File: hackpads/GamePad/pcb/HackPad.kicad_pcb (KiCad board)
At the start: 2 copper layers, 100 x 69 mm, 36 parts, among them J1 OLED_128x64, SW1 SW_Push_45deg, SW10 RotaryEncoder_Switch, SW2 SW_Push_45deg, SW3 SW_Push_45deg, SW4 SW_Push_45deg, SW5 SW_Push_45deg, SW6 SW_Push_45deg, SW7 SW_Push_45deg, SW8 SW_Push_45deg, U1 MOUDLE-SEEEDUINO-XIAO

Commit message: minor edits
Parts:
- moved G*** 0.50 mm to (180.0, 90.5)
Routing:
- net Row 3: track 152.4 -> 160.1 mm, vias 1 -> 0
- net Net-(D16-DOUT): track 74.0 -> 71.7 mm
- net Column 2: track 126.1 -> 127.0 mm
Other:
- board text added: ")"
- board text added: ":"
- board text added: "Thanks Alex!"
- board text removed: "Thanks Alex! :)"

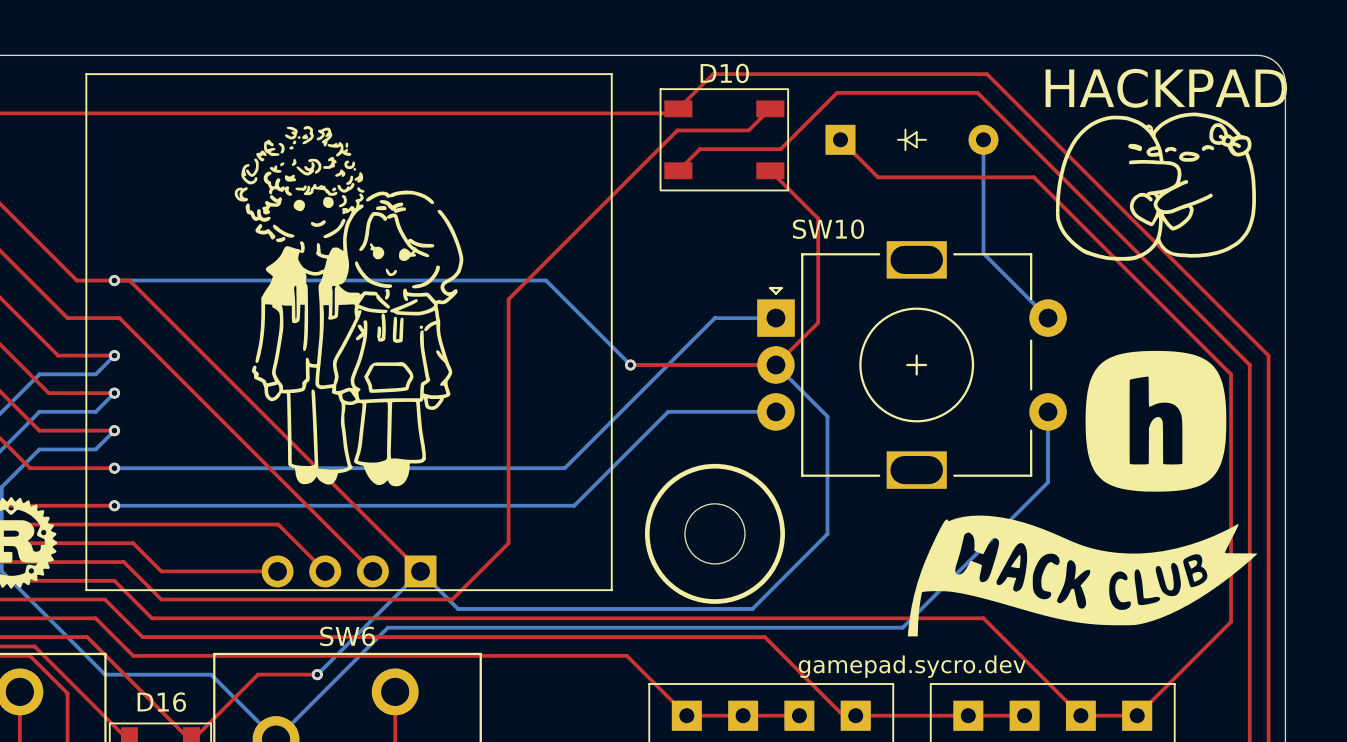
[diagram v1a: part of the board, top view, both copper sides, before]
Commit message: move the rotary encoder right
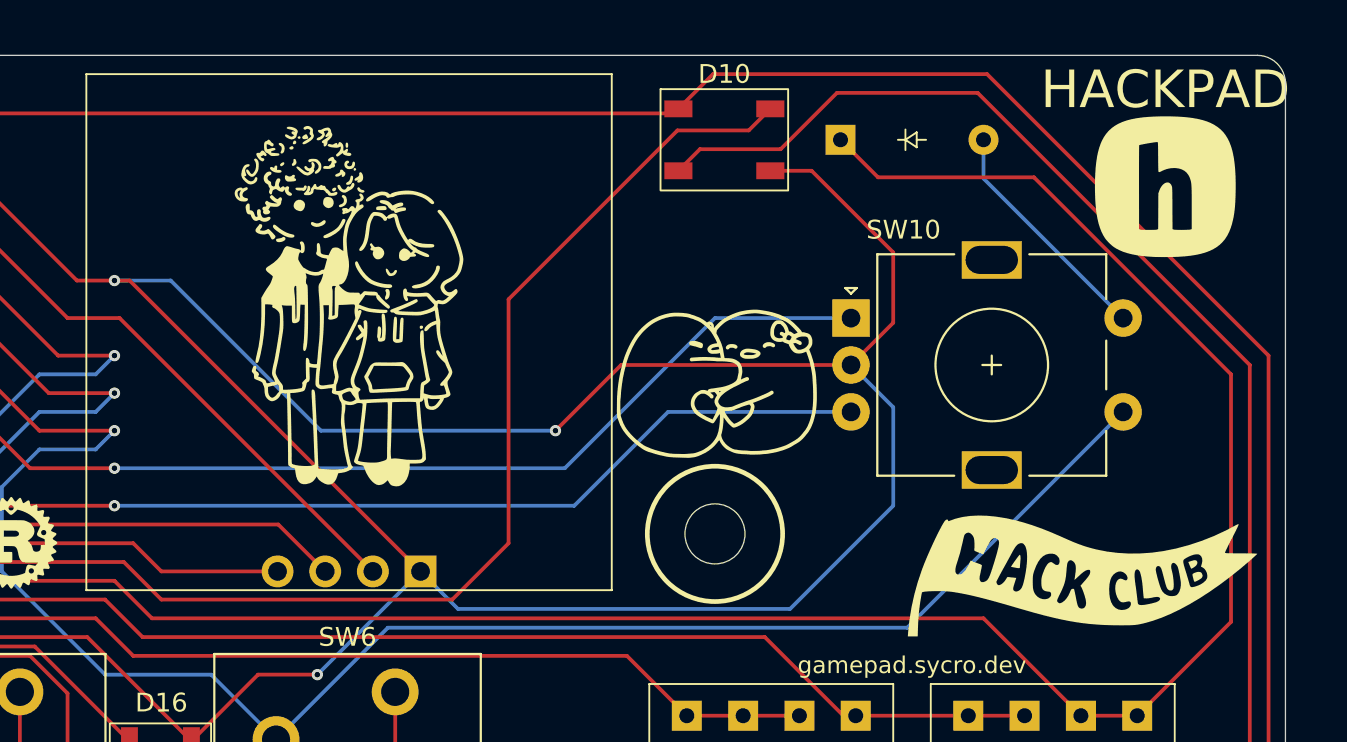
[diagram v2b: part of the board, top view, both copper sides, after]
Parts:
- moved G*** 25.6 mm to (156.8, 87.5)
- moved G*** 12.5 mm to (180.5, 78.0)
- moved SW10 4.00 mm to (163.8, 85.0)
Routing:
- net GND: track 278.2 -> 289.8 mm
- net EC11B: track 75.4 -> 79.4 mm
- net EC11A: track 51.9 -> 55.9 mm
- net Column 3: track 115.0 -> 116.8 mm
- net EC11SWB: track 10.9 -> 12.6 mm
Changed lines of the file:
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@@
 	(footprint "LOGO"
 		(layer "F.Cu")
-		(at 180 90.5)
+		(at 180.5 78)
 		(property "Reference" "G***"
 			(at 0 0 0)
@@
 	(footprint "LOGO"
 		(layer "F.Cu")
-		(at 180.215771 77.038707)
+		(at 156.815771 87.538707)
 		(property "Reference" "G***"
 			(at 0 0 0)
@@
 	(footprint "Rotary_Encoder:RotaryEncoder_Alps_EC11E-Switch_Vertical_H20mm"
 		(layer "F.Cu")
-		(at 159.75 85)
+		(at 163.75 85)
 		(descr "Alps rotary encoder, EC12E... with switch, vertical shaft, http://www.alps.com/prod/info/E/HTML/Encoder/Incremental/EC11/EC11E15204A3.html")
 		(tags "rotary encoder")
@@
 	)
 	(segment
-		(start 174.25 85)
-		(end 170.81 81.56)
+		(start 178.25 85)
+		(end 170.81 77.56)
 		(width 0.2)
 		(layer "B.Cu")
@@
 	)
 	(segment
-		(start 170.81 81.56)
+		(start 170.81 77.56)
 		(end 170.81 75.5)
 		(width 0.2)
@@
 	)
 	(segment
-		(start 162 85.25)
-		(end 159.75 87.5)
-		(width 0.2)
-		(layer "F.Cu")
-		(net 15)
-	)
-	(segment
 		(start 114.625 76.632015)
 		(end 110.492985 72.5)
@@
 	)
 	(segment
+		(start 163.75 87.5)
+		(end 151.5 87.5)
+		(width 0.2)
+		(layer "F.Cu")
+		(net 15)
+	)
+	(segment
 		(start 136.753402 126.51)
 		(end 136.193402 125.95)
@@
 	)
 	(segment
-		(start 162 79.7)
-		(end 162 85.25)
-		(width 0.2)
-		(layer "F.Cu")
-		(net 15)
-	)
-	(segment
 		(start 123.05 102)
 		(end 128.6 107.55)
@@
 	)
 	(segment
+		(start 166 81.5)
+		(end 166 85.25)
+		(width 0.2)
+		(layer "F.Cu")
+		(net 15)
+	)
+	(segment
 		(start 150.7 125.5)
 		(end 148.65 127.55)
@@
 	)
 	(segment
+		(start 166 85.25)
+		(end 163.75 87.5)
+		(width 0.2)
+		(layer "F.Cu")
+		(net 15)
+	)
+	(segment
 		(start 162.5 127)
 		(end 157.592412 127)
@@
 	)
 	(segment
-		(start 110.29 125.91)
-		(end 108.65 127.55)
+		(start 151.5 87.5)
+		(end 148 91)
 		(width 0.2)
 		(layer "F.Cu")
@@
 	)
 	(segment
-		(start 120.053048 126.558984)
-		(end 114.441016 126.558984)
+		(start 110.29 125.91)
+		(end 108.65 127.55)
 		(width 0.2)
 		(layer "F.Cu")
@@
 	)
 	(segment
-		(start 159.75 87.5)
-		(end 152 87.5)
+		(start 120.053048 126.558984)
+		(end 114.441016 126.558984)
 		(width 0.2)
 		(layer "F.Cu")
@@
 	)
 	(segment
+		(start 161.65 77.15)
+		(end 166 81.5)
+		(width 0.2)
+		(layer "F.Cu")
+		(net 15)
+	)
+	(segment
 		(start 148.65 127.55)
 		(end 147.6 126.5)
@@
 	)
 	(segment
-		(start 159.45 77.15)
-		(end 162 79.7)
+		(start 108 117)
+		(end 108 108.3)
 		(width 0.2)
 		(layer "F.Cu")
@@
 	)
 	(segment
-		(start 108 117)
-		(end 108 108.3)
+		(start 125.31 83)
+		(end 140.81 98.5)
 		(width 0.2)
 		(layer "F.Cu")
@@
 	)
 	(segment
-		(start 125.31 83)
-		(end 140.81 98.5)
+		(start 159.45 77.15)
+		(end 161.65 77.15)
 		(width 0.2)
 		(layer "F.Cu")
@@
 	)
 	(via
-		(at 152 87.5)
+		(at 148 91)
 		(size 0.6)
 		(drill 0.3)
@@
 	)
 	(segment
-		(start 147.5 83)
-		(end 124.5 83)
+		(start 148 91)
+		(end 135.5 91)
 		(width 0.2)
 		(layer "B.Cu")
@@
 	)
 	(segment
-		(start 158.5 100.5)
-		(end 142.81 100.5)
+		(start 142.81 100.5)
+		(end 160.5 100.5)
 		(width 0.2)
 		(layer "B.Cu")
@@
 	)
 	(segment
-		(start 162.5 90.25)
-		(end 162.5 96.5)
+		(start 166 95)
+		(end 166 89.75)
 		(width 0.2)
 		(layer "B.Cu")
@@
 	)
 	(segment
-		(start 142.81 100.5)
-		(end 140.81 98.5)
+		(start 135.5 91)
+		(end 127.5 83)
 		(width 0.2)
 		(layer "B.Cu")
@@
 	)
 	(segment
-		(start 159.75 87.5)
-		(end 159 87.5)
+		(start 140.81 98.5)
+		(end 142.81 100.5)
 		(width 0.2)
 		(layer "B.Cu")
@@
 	)
 	(segment
-		(start 152 87.5)
-		(end 147.5 83)
+		(start 127.5 83)
+		(end 124.5 83)
 		(width 0.2)
 		(layer "B.Cu")
@@
 	)
 	(segment
-		(start 162.5 96.5)
-		(end 158.5 100.5)
+		(start 160.5 100.5)
+		(end 166 95)
 		(width 0.2)
 		(layer "B.Cu")
@@
 	)
 	(segment
-		(start 159.75 87.5)
-		(end 162.5 90.25)
+		(start 108 123)
+		(end 108 117)
 		(width 0.2)
 		(layer "B.Cu")
@@
 	)
 	(segment
-		(start 108 123)
-		(end 108 117)
+		(start 166 89.75)
+		(end 163.75 87.5)
 		(width 0.2)
 		(layer "B.Cu")
@@
 	)
 	(segment
-		(start 129.65 104)
+		(start 139.07 101.5)
 		(end 133.11 107.46)
 		(width 0.2)
@@
 	)
 	(segment
-		(start 124.5 91)
-		(end 123.5 92)
+		(start 129.65 104)
+		(end 133.11 107.46)
 		(width 0.2)
 		(layer "B.Cu")
@@
 	)
 	(segment
-		(start 174.25 93.75)
-		(end 166.5 101.5)
+		(start 124.5 91)
+		(end 123.5 92)
 		(width 0.2)
 		(layer "B.Cu")
@@
 	)
 	(segment
-		(start 139.07 101.5)
-		(end 133.11 107.46)
+		(start 178.25 90)
+		(end 166.75 101.5)
 		(width 0.2)
 		(layer "B.Cu")
@@
 	)
 	(segment
-		(start 123.5 92)
-		(end 120.5 92)
+		(start 166.75 101.5)
+		(end 139.07 101.5)
 		(width 0.2)
 		(layer "B.Cu")
@@
 	)
 	(segment
-		(start 174.25 90)
-		(end 174.25 93.75)
+		(start 123.5 92)
+		(end 120.5 92)
 		(width 0.2)
 		(layer "B.Cu")
@@
 	)
 	(segment
-		(start 166.5 101.5)
-		(end 139.07 101.5)
-		(width 0.2)
-		(layer "B.Cu")
-		(net 23)
-	)
-	(segment
 		(start 96 95)
 		(end 124.5 95)
@@
 	)
 	(segment
-		(start 149 95)
-		(end 154 90)
+		(start 154 90)
+		(end 163.75 90)
 		(width 0.2)
 		(layer "B.Cu")
@@
 	)
 	(segment
-		(start 124.5 95)
-		(end 149 95)
+		(start 149 95)
+		(end 154 90)
 		(width 0.2)
 		(layer "B.Cu")
@@
 	)
 	(segment
-		(start 154 90)
-		(end 159.75 90)
+		(start 124.5 95)
+		(end 149 95)
 		(width 0.2)
 		(layer "B.Cu")
@@
 	)
 	(segment
-		(start 156.5 85)
-		(end 159.75 85)
+		(start 124.5 93)
+		(end 148.5 93)
 		(width 0.2)
 		(layer "B.Cu")
@@
 	)
 	(segment
-		(start 124.5 93)
-		(end 148.5 93)
+		(start 156.5 85)
+		(end 163.75 85)
 		(width 0.2)
 		(layer "B.Cu")

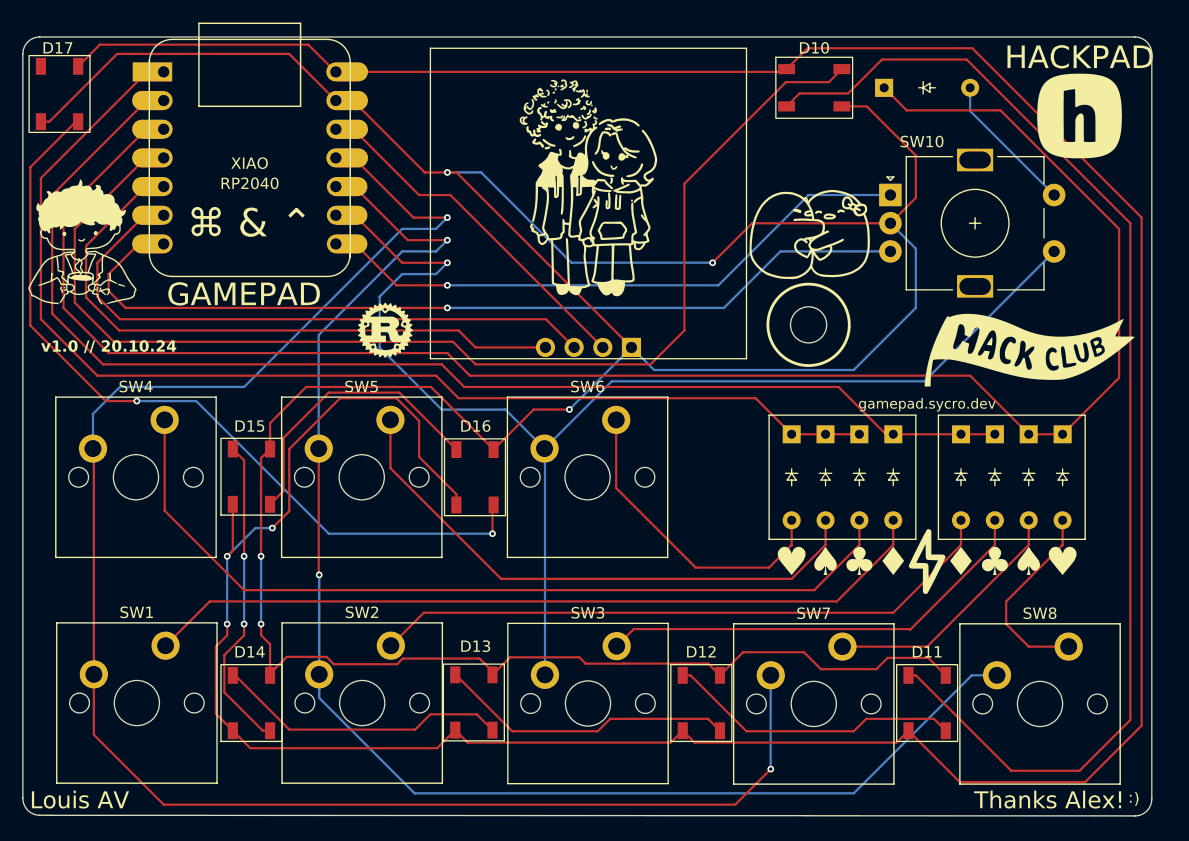
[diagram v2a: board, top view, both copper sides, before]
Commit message: fix the pin height issue
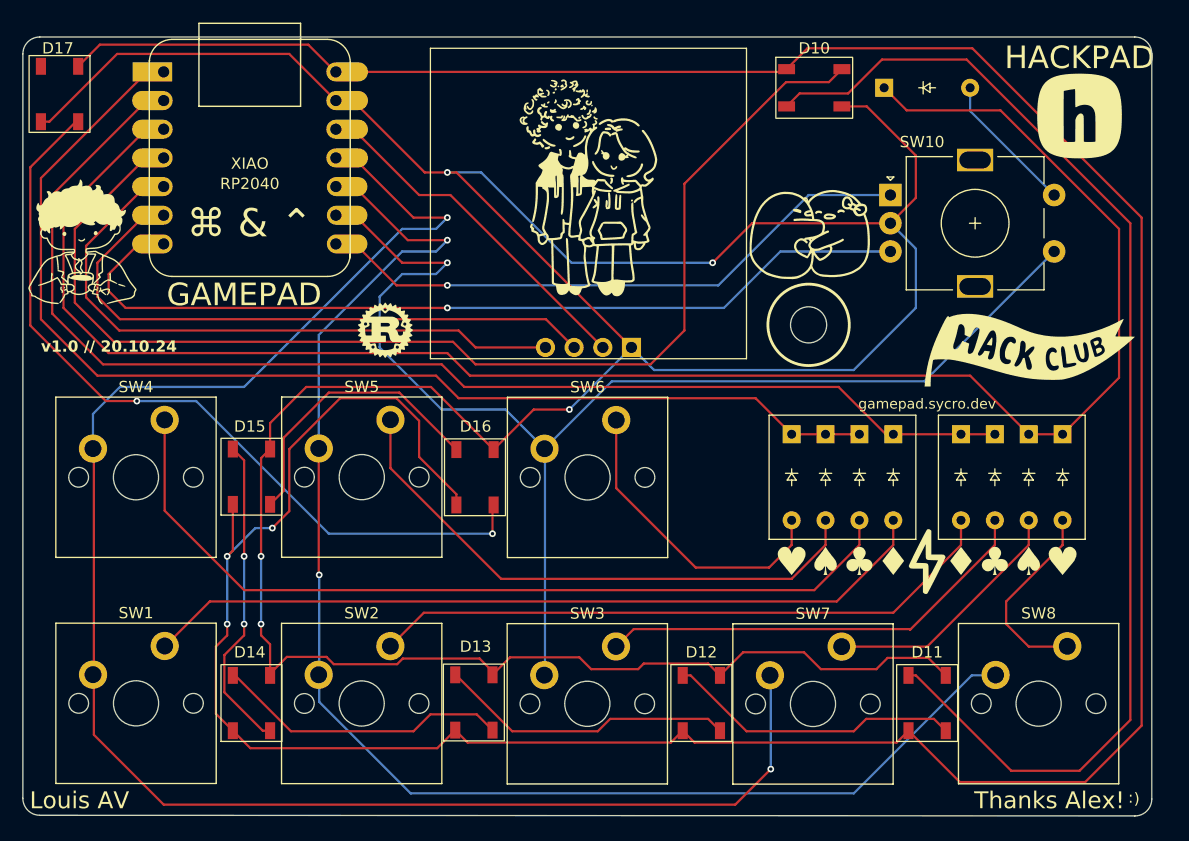
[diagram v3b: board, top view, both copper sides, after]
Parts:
- moved SW8 0.13 mm to (176.9, 130.1)
- moved SW1 0.08 mm to (96.9, 130.0)
- moved SW7 0.07 mm to (156.9, 130.1)
- moved SW3 0.07 mm to (136.9, 130.1)
- moved SW2 0.06 mm to (116.9, 130.0)
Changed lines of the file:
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@@
 		(pad_to_mask_clearance 0)
 		(allow_soldermask_bridges_in_footprints no)
+		(grid_origin 86.9 71)
 		(pcbplotparams
 			(layerselection 0x00010fc_ffffffff)
@@
 	(footprint "ScottoKeebs_MX:MX_PCB_1.00u"
 		(layer "F.Cu")
-		(at 156.96 130.08)
+		(at 156.8875 130.08)
 		(descr "MX keyswitch PCB Mount Keycap 1.00u")
 		(tags "MX Keyboard Keyswitch Switch PCB Cutout Keycap 1.00u")
@@
 	(footprint "ScottoKeebs_MX:MX_PCB_1.00u"
 		(layer "F.Cu")
-		(at 97 130)
+		(at 96.925 130.025)
 		(descr "MX keyswitch PCB Mount Keycap 1.00u")
 		(tags "MX Keyboard Keyswitch Switch PCB Cutout Keycap 1.00u")
@@
 	(footprint "ScottoKeebs_MX:MX_PCB_1.00u"
 		(layer "F.Cu")
-		(at 116.92 110)
+		(at 116.92 109.9875)
 		(descr "MX keyswitch PCB Mount Keycap 1.00u")
 		(tags "MX Keyboard Keyswitch Switch PCB Cutout Keycap 1.00u")
@@
 	(footprint "ScottoKeebs_MX:MX_PCB_1.00u"
 		(layer "F.Cu")
-		(at 136.92 110)
+		(at 136.92 110.0125)
 		(descr "MX keyswitch PCB Mount Keycap 1.00u")
 		(tags "MX Keyboard Keyswitch Switch PCB Cutout Keycap 1.00u")
@@
 	(footprint "ScottoKeebs_MX:MX_PCB_1.00u"
 		(layer "F.Cu")
-		(at 116.96 130)
+		(at 116.9125 130.03875)
 		(descr "MX keyswitch PCB Mount Keycap 1.00u")
 		(tags "MX Keyboard Keyswitch Switch PCB Cutout Keycap 1.00u")
@@
 	(footprint "ScottoKeebs_MX:MX_PCB_1.00u"
 		(layer "F.Cu")
-		(at 177 130.08)
+		(at 176.875 130.0525)
 		(descr "MX keyswitch PCB Mount Keycap 1.00u")
 		(tags "MX Keyboard Keyswitch Switch PCB Cutout Keycap 1.00u")
@@
 	(footprint "ScottoKeebs_MX:MX_PCB_1.00u"
 		(layer "F.Cu")
-		(at 136.96 130.04)
+		(at 136.9 130.06625)
 		(descr "MX keyswitch PCB Mount Keycap 1.00u")
 		(tags "MX Keyboard Keyswitch Switch PCB Cutout Keycap 1.00u")
@@
 	)
 	(segment
-		(start 147.6 126.5)
-		(end 140.152032 126.5)
+		(start 157.592412 127)
+		(end 156.092412 125.5)
 		(width 0.2)
 		(layer "F.Cu")
@@
 	)
 	(segment
-		(start 130.05 125.95)
-		(end 128.5 127.5)
+		(start 137.243402 127)
+		(end 136.193402 125.95)
 		(width 0.2)
 		(layer "F.Cu")
@@
 	)
 	(segment
+		(start 150.7 125.5)
+		(end 148.65 127.55)
+		(width 0.2)
+		(layer "F.Cu")
+		(net 15)
+	)
+	(segment
 		(start 132.15 104)
 		(end 128.6 107.55)
@@
 	)
 	(segment
-		(start 136.753402 126.51)
-		(end 136.193402 125.95)
+		(start 130.05 125.95)
+		(end 128.5 127.5)
 		(width 0.2)
 		(layer "F.Cu")
@@
 	)
 	(segment
-		(start 157.592412 127)
-		(end 156.092412 125.5)
+		(start 141.4 127)
+		(end 137.243402 127)
+		(width 0.2)
+		(layer "F.Cu")
+		(net 15)
+	)
+	(segment
+		(start 167.1 126)
+		(end 163.5 126)
 		(width 0.2)
 		(layer "F.Cu")
@@
 	)
 	(segment
-		(start 123.05 102)
-		(end 128.6 107.55)
+		(start 141.9 126.5)
+		(end 141.4 127)
 		(width 0.2)
 		(layer "F.Cu")
@@
 	)
 	(segment
-		(start 113.792032 125.91)
-		(end 110.29 125.91)
+		(start 123.05 102)
+		(end 128.6 107.55)
 		(width 0.2)
 		(layer "F.Cu")
@@
 	)
 	(segment
-		(start 136.193402 125.95)
-		(end 130.05 125.95)
+		(start 113.792032 125.91)
+		(end 110.29 125.91)
 		(width 0.2)
 		(layer "F.Cu")
@@
 	)
 	(segment
-		(start 140.142032 126.51)
-		(end 136.753402 126.51)
+		(start 163.5 126)
+		(end 162.5 127)
 		(width 0.2)
 		(layer "F.Cu")
@@
 	)
 	(segment
-		(start 156.092412 125.5)
-		(end 150.7 125.5)
+		(start 148.65 127.55)
+		(end 147.6 126.5)
 		(width 0.2)
 		(layer "F.Cu")
@@
 	)
 	(segment
-		(start 167.1 126)
-		(end 163.5 126)
+		(start 166 81.5)
+		(end 166 85.25)
 		(width 0.2)
 		(layer "F.Cu")
@@
 	)
 	(segment
-		(start 166 81.5)
-		(end 166 85.25)
+		(start 114.441016 126.558984)
+		(end 113.792032 125.91)
 		(width 0.2)
 		(layer "F.Cu")
@@
 	)
 	(segment
-		(start 150.7 125.5)
-		(end 148.65 127.55)
+		(start 124.5 83)
+		(end 122.5 83)
 		(width 0.2)
 		(layer "F.Cu")
@@
 	)
 	(segment
-		(start 114.441016 126.558984)
-		(end 113.792032 125.91)
+		(start 108 108.3)
+		(end 108.8 107.5)
 		(width 0.2)
 		(layer "F.Cu")
@@
 	)
 	(segment
-		(start 163.5 126)
-		(end 162.5 127)
+		(start 166 85.25)
+		(end 163.75 87.5)
 		(width 0.2)
 		(layer "F.Cu")
@@
 	)
 	(segment
-		(start 124.5 83)
-		(end 122.5 83)
+		(start 95.25 72.5)
+		(end 89.25 78.5)
 		(width 0.2)
 		(layer "F.Cu")
@@
 	)
 	(segment
-		(start 108 108.3)
-		(end 108.8 107.5)
+		(start 156.092412 125.5)
+		(end 150.7 125.5)
 		(width 0.2)
 		(layer "F.Cu")
@@
 	)
 	(segment
-		(start 166 85.25)
-		(end 163.75 87.5)
+		(start 147.6 126.5)
+		(end 141.9 126.5)
 		(width 0.2)
 		(layer "F.Cu")
@@
 	)
 	(segment
-		(start 95.25 72.5)
-		(end 89.25 78.5)
+		(start 116.132015 76.632015)
+		(end 114.625 76.632015)
 		(width 0.2)
 		(layer "F.Cu")
@@
 	)
 	(segment
-		(start 116.132015 76.632015)
-		(end 114.625 76.632015)
+		(start 151.5 87.5)
+		(end 148 91)
 		(width 0.2)
 		(layer "F.Cu")
@@
 	)
 	(segment
-		(start 151.5 87.5)
-		(end 148 91)
+		(start 136.193402 125.95)
+		(end 130.05 125.95)
 		(width 0.2)
 		(layer "F.Cu")
@@
 	)
 	(segment
-		(start 148.65 127.55)
-		(end 147.6 126.5)
-		(width 0.2)
-		(layer "F.Cu")
-		(net 15)
-	)
-	(segment
-		(start 140.152032 126.5)
-		(end 140.142032 126.51)
-		(width 0.2)
-		(layer "F.Cu")
-		(net 15)
-	)
-	(segment
 		(start 128.5 127.5)
 		(end 128.5 127.2)
@@
 	)
 	(segment
-		(start 121.65 132.35)
-		(end 110.5 132.35)
+		(start 121.5 132.5)
+		(end 110.65 132.5)
 		(width 0.2)
 		(layer "F.Cu")
@@
 	)
 	(segment
-		(start 105.7 127.55)
-		(end 105.5 127.55)
+		(start 127.1 131)
+		(end 123 131)
 		(width 0.2)
 		(layer "F.Cu")
@@
 	)
 	(segment
-		(start 127.1 131)
-		(end 123 131)
+		(start 110.65 132.5)
+		(end 105.7 127.55)
 		(width 0.2)
 		(layer "F.Cu")
@@
 	)
 	(segment
-		(start 128.5 132.4)
-		(end 127.1 131)
+		(start 105.7 127.55)
+		(end 105.5 127.55)
 		(width 0.2)
 		(layer "F.Cu")
@@
 	(segment
 		(start 123 131)
-		(end 121.65 132.35)
+		(end 121.5 132.5)
 		(width 0.2)
 		(layer "F.Cu")
@@
 	)
 	(segment
-		(start 110.5 132.35)
-		(end 105.7 127.55)
+		(start 128.5 132.4)
+		(end 127.1 131)
 		(width 0.2)
 		(layer "F.Cu")
@@
 	)
 	(segment
-		(start 93.19 127.46)
-		(end 93.19 107.54)
+		(start 153.15 135.85)
+		(end 150 139)
 		(width 0.2)
 		(layer "F.Cu")
@@
 	)
 	(segment
-		(start 150 139)
-		(end 99.38 139)
+		(start 93.19 107.54)
+		(end 93.11 107.46)
 		(width 0.2)
 		(layer "F.Cu")
@@
 	(segment
 		(start 93.19 132.81)
-		(end 93.19 127.46)
-		(width 0.2)
-		(layer "F.Cu")
-		(net 22)
-	)
-	(segment
-		(start 99.38 139)
-		(end 93.19 132.81)
+		(end 93.19 107.54)
 		(width 0.2)
 		(layer "F.Cu")
@@
 	)
 	(segment
-		(start 93.19 107.54)
-		(end 93.11 107.46)
+		(start 99.38 139)
+		(end 93.19 132.81)
 		(width 0.2)
 		(layer "F.Cu")
@@
 	)
 	(segment
-		(start 153.15 135.85)
-		(end 150 139)
+		(start 150 139)
+		(end 99.38 139)
 		(width 0.2)
 		(layer "F.Cu")
@@
 	)
 	(segment
-		(start 113.15 118.65)
-		(end 113.15 127.46)
+		(start 113.15 129.893794)
+		(end 113.15 118.65)
 		(width 0.2)
 		(layer "B.Cu")
@@
 	)
 	(segment
-		(start 160.5 138)
-		(end 121.612412 138)
+		(start 121.256206 138)
+		(end 113.15 129.893794)
 		(width 0.2)
 		(layer "B.Cu")
@@
 	)
 	(segment
-		(start 170.96 127.54)
-		(end 160.5 138)
+		(start 173.19 127.54)
+		(end 170.96 127.54)
 		(width 0.2)
 		(layer "B.Cu")
@@
 	)
 	(segment
-		(start 113.15 129.537588)
-		(end 113.15 127.46)
+		(start 113.11 97.39)
+		(end 113.11 107.46)
 		(width 0.2)
 		(layer "B.Cu")
@@
 	)
 	(segment
-		(start 113.11 97.39)
+		(start 113.15 107.5)
 		(end 113.11 107.46)
 		(width 0.2)
@@
 	)
 	(segment
-		(start 121.612412 138)
-		(end 113.15 129.537588)
+		(start 160.5 138)
+		(end 121.256206 138)
 		(width 0.2)
 		(layer "B.Cu")
@@
 	)
 	(segment
-		(start 113.15 107.5)
-		(end 113.11 107.46)
+		(start 170.96 127.54)
+		(end 160.5 138)
 		(width 0.2)
 		(layer "B.Cu")
@@
 		(width 0.2)
 		(layer "B.Cu")
-		(net 27)
-	)
-	(segment
-		(start 173.19 127.54)
-		(end 170.96 127.54)
-		(width 0.2)
-		(layer "B.Cu")
